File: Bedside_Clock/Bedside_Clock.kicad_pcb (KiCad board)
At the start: 4 copper layers, 177.8 x 68.6 mm, 198 parts, among them J1 USBC_USB2.0, U1 ESP32-C3-MINI-1, U2 USBLC6-2SC6

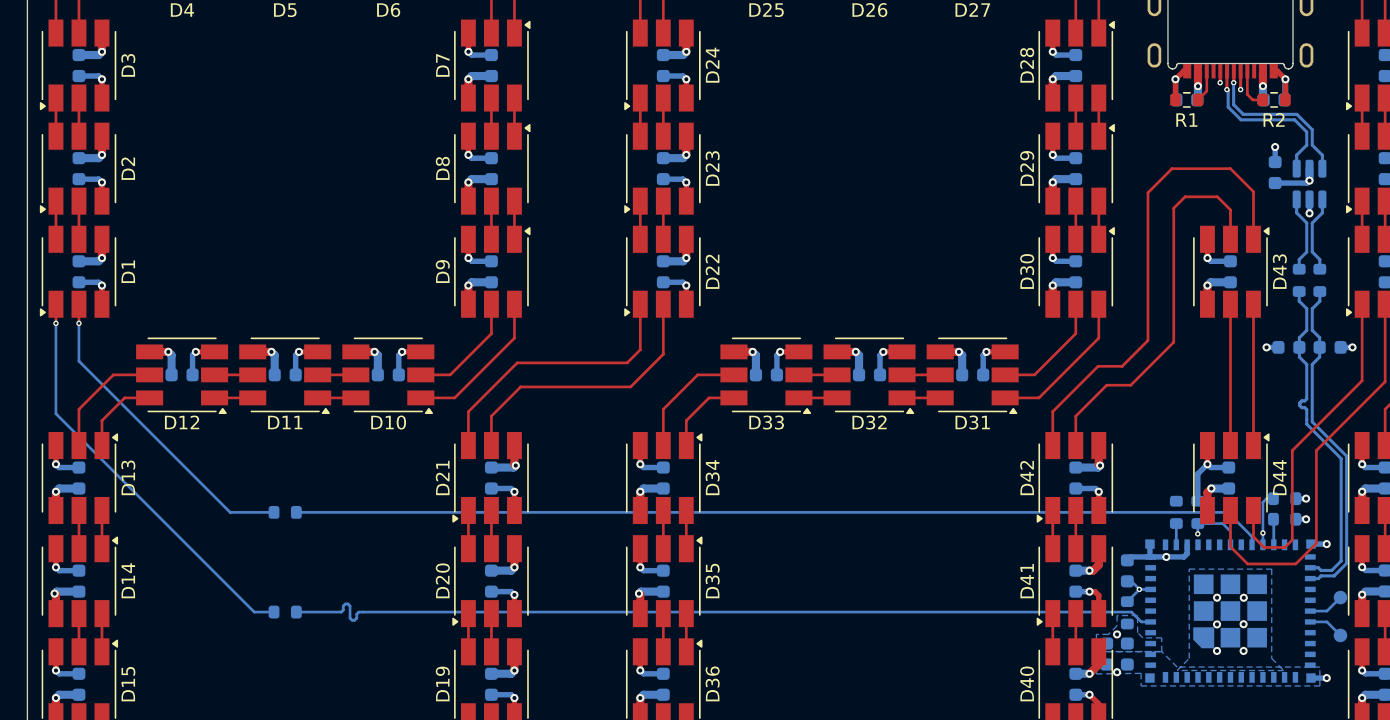
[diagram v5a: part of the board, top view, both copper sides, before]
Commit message: [HW] Add Ambient Light Sensor and Level Shifter
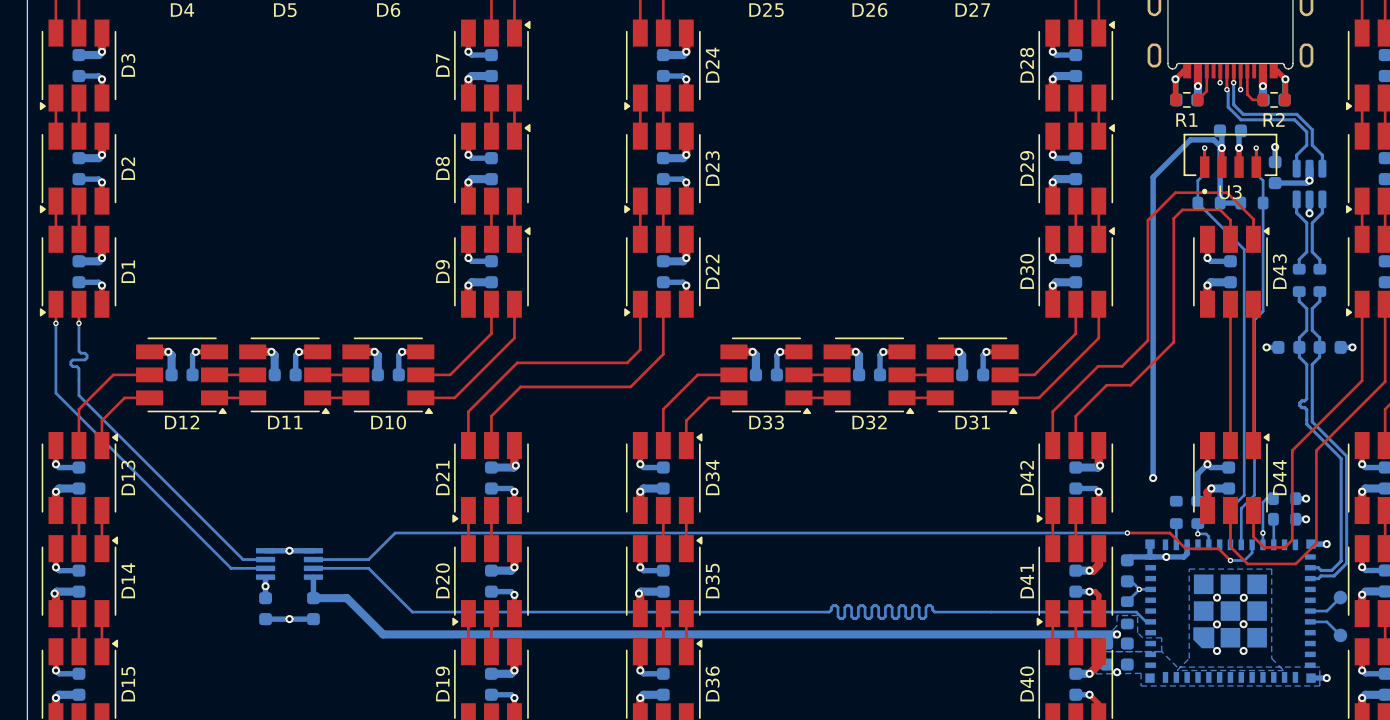
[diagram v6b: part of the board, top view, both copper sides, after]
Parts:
- added C97: 100nF, Capacitor_SMD:C_0603_1608Metric, B.Cu at (120.7, 53.1)
- added C98: 10uF, Capacitor_SMD:C_0603_1608Metric, B.Cu at (49.3, 88.4)
- added C99: 100nF, Capacitor_SMD:C_0603_1608Metric, B.Cu at (52.9, 88.4)
- added U3: VEML7700-TT, VEML7700_TT:XDCR_VEML7700-TT, F.Cu at (120.7, 54.9)
- added U4: SN74LVC2T45DCUR, SN74LVC2T45DCTR:SOP65P400X130-8N, B.Cu at (51.1, 85.1)
- R10, R11: value 0 -> 5.1k
- moved R11 75.0 mm to (122.2, 58.4)
- moved R10 74.7 mm to (119.1, 58.4), turned to 0 degrees
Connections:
- net Net-(J1-CC1) renamed /CC1
- net Net-(J1-CC2) renamed /CC2
- R10 pad 1: /DO -> /SCL
- R10 pad 2: /Digit0/DI -> +3V3
- R11 pad 1: /CO -> /SDA
- R11 pad 2: /Digit0/CI -> +3V3
- U1 pad 16: unconnected-(U1-GPIO10-Pad16) -> /COLOR
- U1 pad 18: /COLOR -> /SCL
- U1 pad 19: unconnected-(U1-GPIO5/ADC2_CH0-Pad19) -> /SDA
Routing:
- net +3V3: track 0.76 -> 99.9 mm, vias 2 -> 4
- net /SCL: track 0.00 -> 32.8 mm, vias 0 -> 1
- net /SDA: track 0.00 -> 31.6 mm, vias 0 -> 1
- net GND: track 299.4 -> 309.2 mm, vias 103 -> 106
- net /DO: track 65.3 -> 75.0 mm
- net /Digit0/CI: track 23.2 -> 27.4 mm
- net /Digit1/DO: track 35.4 -> 31.5 mm
- net /Digit0/DI: track 30.3 -> 27.4 mm
- net /COLOR: track 4.41 -> 2.26 mm
- net /Digit1/CO: track 28.7 -> 27.0 mm
- net +5V: track 281.8 -> 283.3 mm, vias 89 -> 90
- net /CO: track 72.0 -> 71.9 mm, vias 0 -> 2

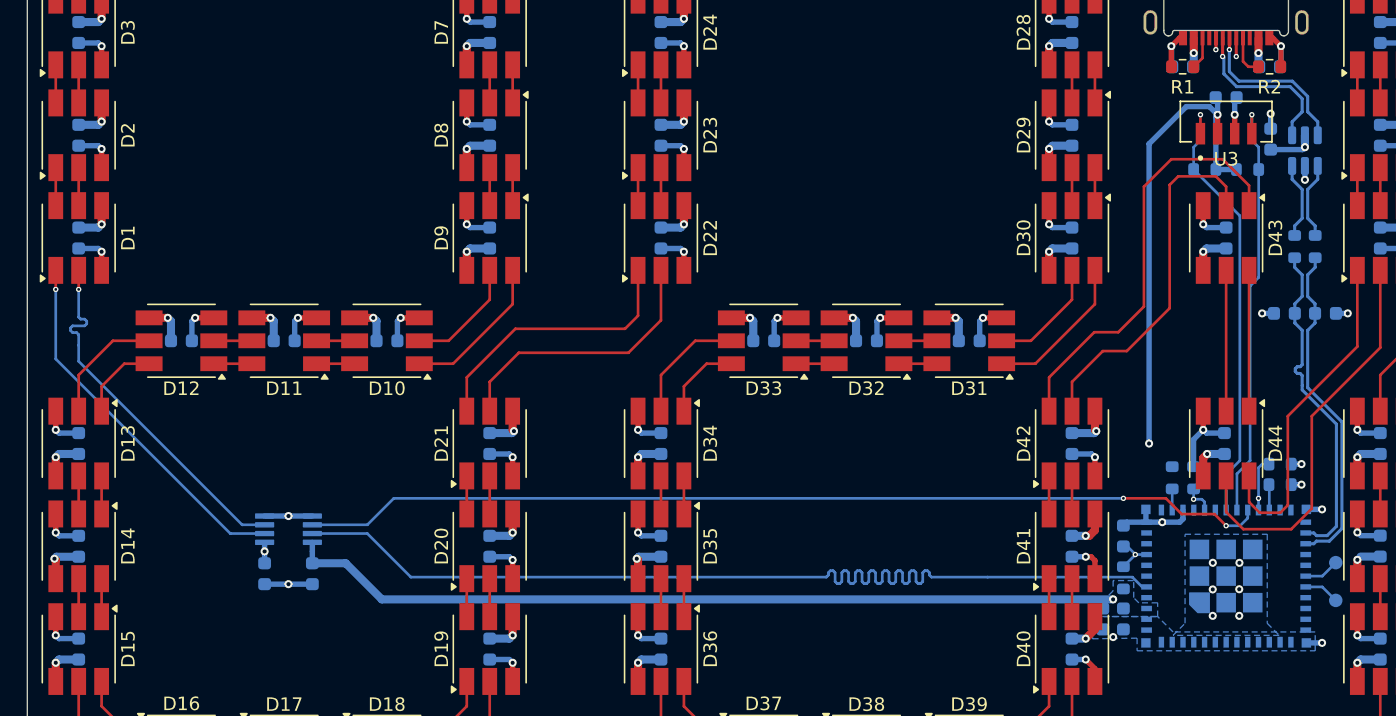
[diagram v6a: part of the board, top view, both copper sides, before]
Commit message: [HW] Switch Ambient Light sensor to have proximity
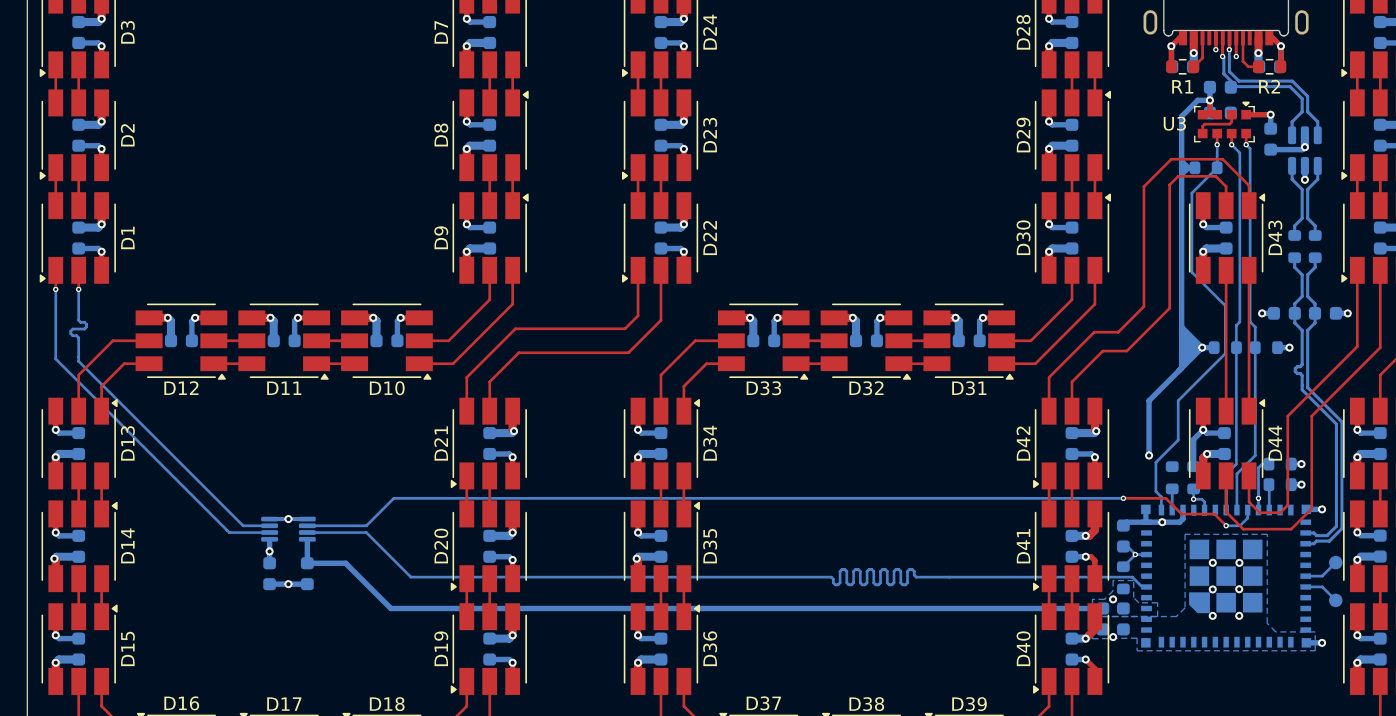
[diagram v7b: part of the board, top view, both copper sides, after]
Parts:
- removed the C97 at (120.7, 53.1)
- added C100: 2.2uF, Capacitor_SMD:C_0603_1608Metric, B.Cu at (120.2, 54.2)
- added C99: 100nF, Capacitor_SMD:C_0603_1608Metric, B.Cu at (120.2, 52.3)
- added R12: 8k2, Resistor_SMD:R_0603_1608Metric, B.Cu at (119.2, 58.3)
- R1, R2: value 5.1k -> 5k1
- R10, R11: value 5.1k -> 2k2
- U3: value VEML7700-TT -> VCNL4040M3OE; footprint VEML7700_TT:XDCR_VEML7700-TT -> VCNL4040M3OE:VISHAY_VCNL4040_4X2X1.1
- U4: footprint SN74LVC2T45DCTR:SOP65P400X130-8N -> Package_SO:VSSOP-8_2.3x2mm_P0.5mm
- moved R10 13.3 mm to (120.6, 71.6), turned to 180 degrees
- moved R11 13.3 mm to (123.6, 71.6), turned to 0 degrees
- moved C97 0.37 mm to (49.7, 88.4)
- moved C98 0.37 mm to (52.5, 88.4)
- moved U3 0.23 mm to (120.5, 55.1), turned to -90 degrees
- renumbered C98 to C97, C99 to C98
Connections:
- net /CC1 renamed Net-(J1-CC1)
- net /CC2 renamed Net-(J1-CC2)
- R10 pad 1: /SCL -> /SDA
- R11 pad 1: /SDA -> /SCL
- U1 pad 12: unconnected-(U1-GPIO0/ADC1_CH0/XTAL_32K_P-Pad12) -> /PROX_INT
- U1 pad 18: /SCL -> /SDA
- U1 pad 19: /SDA -> /SCL
- U3 pad 1: /SCL -> GND
- U3 pad 2: +3V3 -> Net-(U3-Pad2)
- U3 pad 3: GND -> +3V3
- U3 pad 4: /SDA -> +3V3
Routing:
- net /PROX_INT: track 0.00 -> 32.0 mm, vias 0 -> 1
- net +3V3: track 99.9 -> 109.1 mm, vias 4 -> 6
- net /SCL: track 32.8 -> 28.8 mm
- net Net-(U3-Pad2): track 0.00 -> 3.37 mm
- net /SDA: track 31.6 -> 28.6 mm
- net GND: track 309.2 -> 306.8 mm, vias 106 -> 105

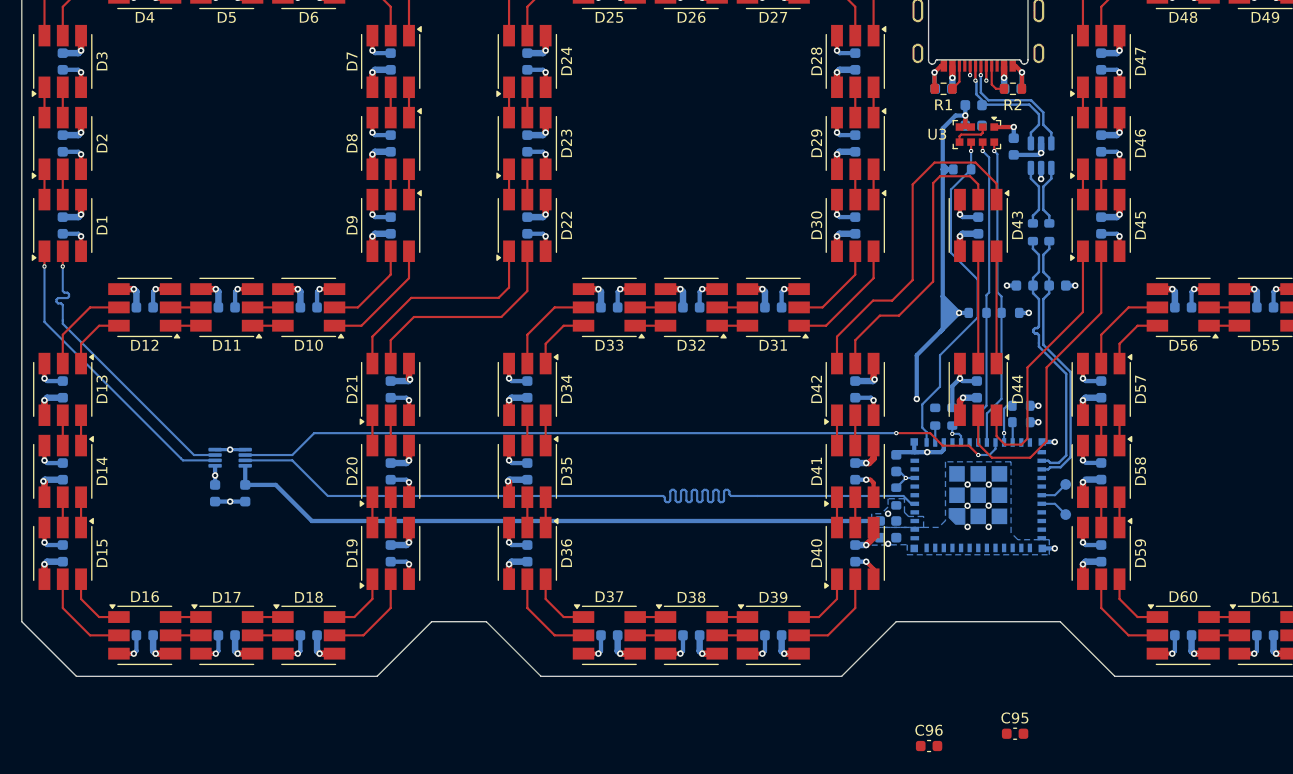
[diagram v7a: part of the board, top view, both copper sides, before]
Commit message: [HW] Find all parts and finish layout
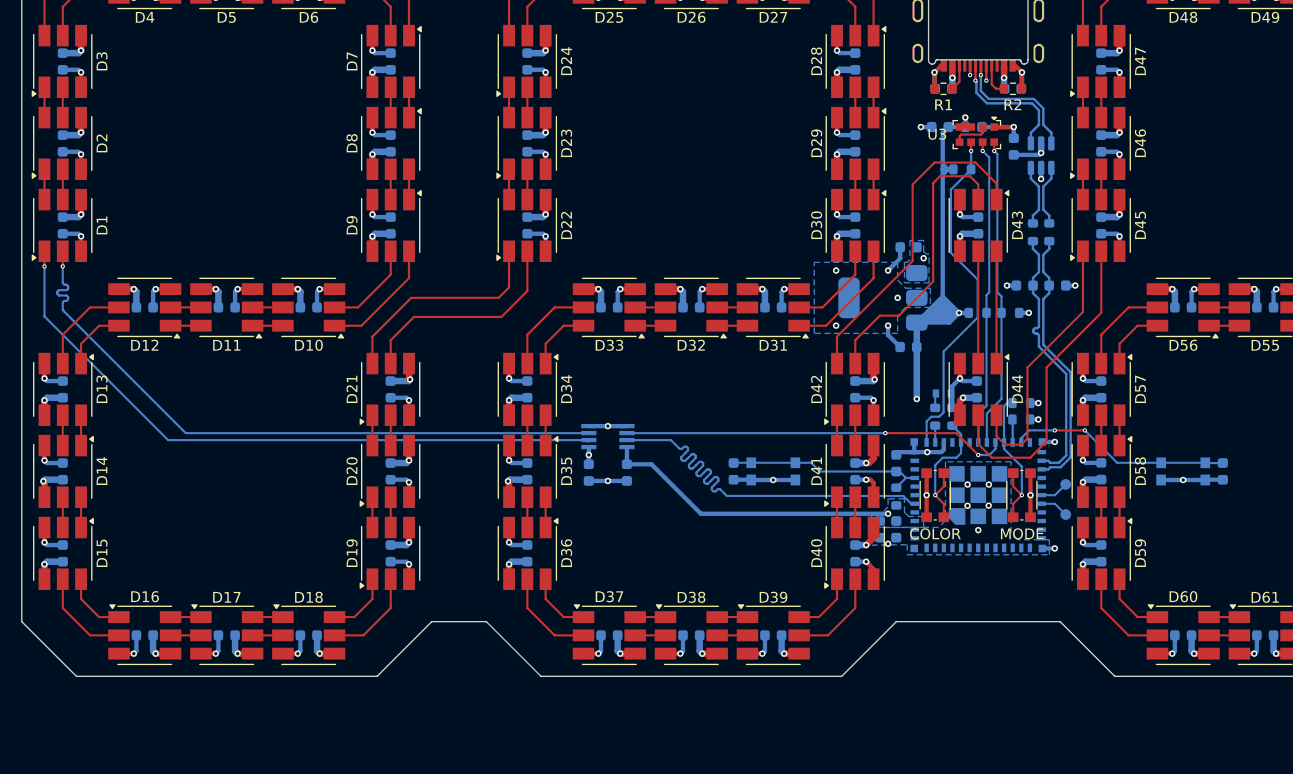
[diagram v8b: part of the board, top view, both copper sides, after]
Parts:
- added C101: 4.7uF, Capacitor_SMD:C_0603_1608Metric, B.Cu at (114.2, 65.5)
- added C102: 1uF, Capacitor_SMD:C_0603_1608Metric, B.Cu at (114.2, 74.8)
- added D87: WL-SMCD_0603, 150060VS55040:WL-SMCD_0603, B.Cu at (117.4, 79.1)
- added SW1: COLOR, TL6330AF200Q:SW_TL6330AF200Q, F.Cu at (116.7, 88.6)
- added SW2: MODE, TL6330AF200Q:SW_TL6330AF200Q, F.Cu at (124.7, 88.6)
- added SW3: BOOT, TL6330AF200Q:SW_TL6330AF200Q, B.Cu at (139.7, 86.4)
- added SW4: RESET, TL6330AF200Q:SW_TL6330AF200Q, B.Cu at (101.6, 86.4)
- added U5: MCP1825S, Package_TO_SOT_SMD:SOT-223-3_TabPin2, B.Cu at (111.8, 70.2)
- C95, C96: moved to B.Cu
- U4: value SN74LVC2T45DCUR -> SN74LVC2T45DCTR; footprint Package_SO:VSSOP-8_2.3x2mm_P0.5mm -> SN74LVC2T45DCTR:SOP65P400X130-8N
- moved C98 35.5 mm to (88.0, 86.5)
- moved U4 35.2 mm to (86.2, 83.1)
- moved C97 34.8 mm to (84.5, 86.5)
- moved C96 31.3 mm to (97.9, 86.4), turned to -90 degrees
- moved C95 31.1 mm to (143.4, 86.4), turned to -90 degrees
- moved C99 3.73 mm to (117.1, 54.4), turned to 180 degrees
- moved R4 0.25 mm to (124.7, 81.5)
- moved R9 0.25 mm to (124.7, 80.0)
- moved C100 0.13 mm to (120.2, 54.4)
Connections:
- net Net-(J1-CC1) renamed /CC1
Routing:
- net /CO: track 72.3 -> 35.9 mm
- net /DO: track 75.4 -> 39.0 mm
- net /Digit0/DI: track 27.8 -> 61.6 mm
- net /Digit0/CI: track 27.8 -> 61.4 mm
- net +3V3: track 109.1 -> 83.4 mm, vias 6 -> 8
- net GND: track 306.8 -> 328.4 mm, vias 105 -> 112
- net /BOOT: track 0.00 -> 20.7 mm, vias 0 -> 2
- net /CHIP_EN: track 3.24 -> 18.4 mm, vias 1 -> 0
- net /COLOR: track 2.26 -> 13.3 mm
- net /MODE: track 4.03 -> 14.6 mm
- net Net-(D87-Pad2): track 0.00 -> 1.36 mm
- net /Digit1/DO: track 31.5 -> 30.5 mm
- net +5V: track 283.6 -> 283.3 mm, vias 90 -> 91
- added copper zone on B.Cu, net +5V
